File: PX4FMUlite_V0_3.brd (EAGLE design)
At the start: 48.6 x 34.9 mm, 143 parts, among them J2 DF13-4P-1.25V, J201 DF13C-6P-1.25V, J202 DF13C-6P-1.25V, J203 DF13C-6P-1.25V, J3 DF13C-4P-1.25V, J302 DF13C-4P-1.25V, J401 DF13C-4P-1.25V, J403 DF13C-7P-1.25V, J405 DF13C-4P-1.25V, J802 DF13C-3P-1.25V, M3_MOUNT1101 MOUNT-HOLE3.1MM, M3_MOUNT1102 MOUNT-HOLE3.1MM, M3_MOUNT1103 MOUNT-HOLE3.1MM, M3_MOUNT1104 MOUNT-HOLE3.1MM, U101 STM32F4X7VX, U2 MAX3051, U401 MAX3051, X101 3.2x2.5 mm / 24 MHz / 15 ppm

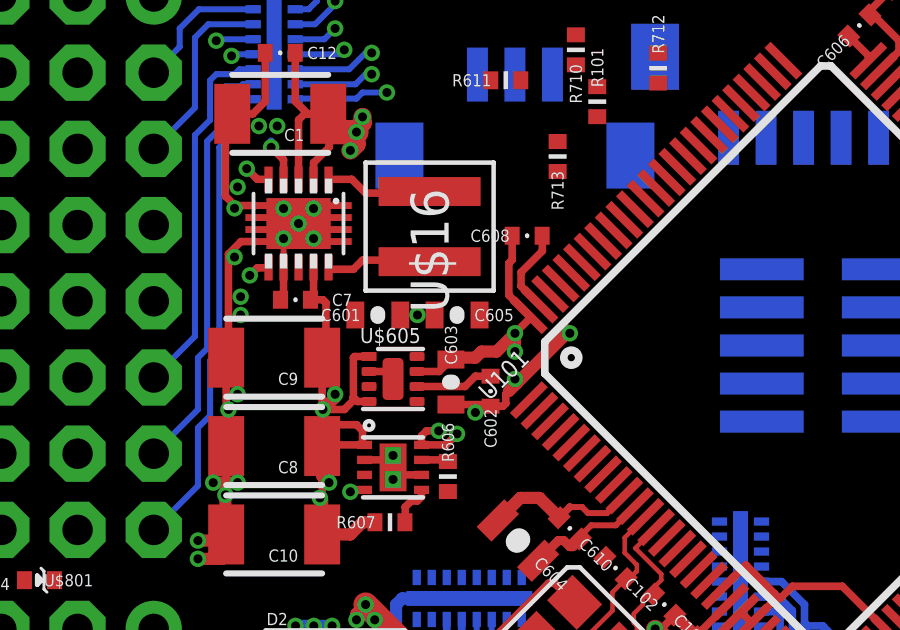
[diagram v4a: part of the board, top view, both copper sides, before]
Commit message: Spektrum 3V3 power routing half done
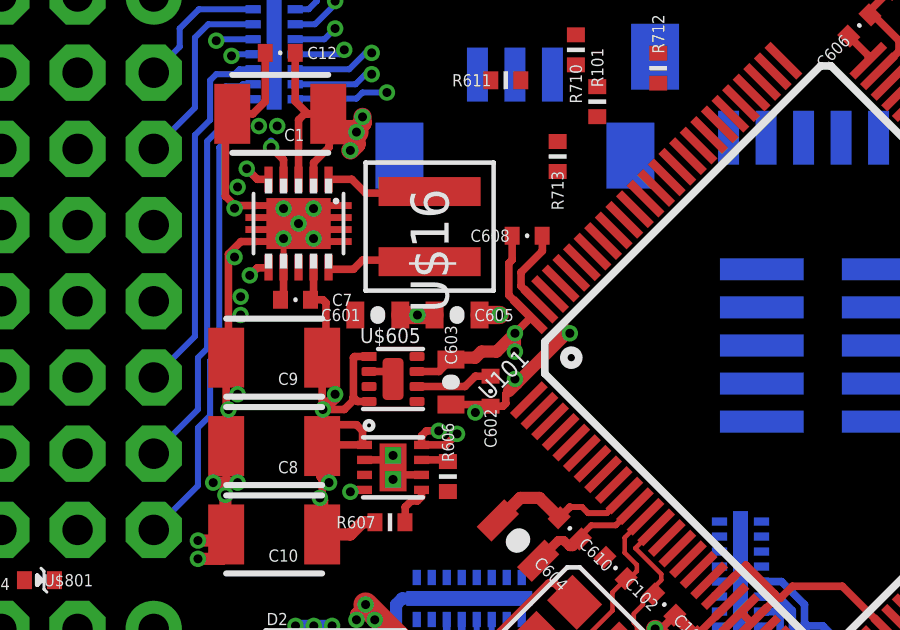
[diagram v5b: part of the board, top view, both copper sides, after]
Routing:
- net GND: track 122.7 -> 123.8 mm
- net VDD_3V3_SPEKTRUM: track 0.00 -> 0.67 mm, vias 0 -> 1
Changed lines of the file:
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@@
 <contactref element="U$801" pad="C"/>
 <contactref element="U$14" pad="2"/>
+<via x="27.5336" y="20.32" extent="1-16" drill="0.3"/>
+<wire x1="26.8612" y1="20.32" x2="27.5336" y2="20.32" width="0.6096" layer="1"/>
 <wire x1="24.7776" y1="18.9364" x2="26.8612" y2="20.32" width="0" layer="19" extent="1-1"/>
 <wire x1="12.692" y1="11.4808" x2="24.7776" y2="18.9364" width="0" layer="19" extent="1-1"/>
@@
 <wire x1="28.0416" y1="18.0848" x2="28.0924" y2="18.034" width="0.4064" layer="1"/>
 <wire x1="29.7688" y1="19.7104" x2="29.8704" y2="19.7104" width="0.4064" layer="1"/>
+<wire x1="19.9136" y1="8.4248" x2="19.0928" y2="8.4248" width="0.4064" layer="16"/>
+<wire x1="19.0928" y1="8.4248" x2="18.8976" y2="8.2296" width="0.4064" layer="16"/>
+<wire x1="18.8976" y1="8.2296" x2="18.8976" y2="7.4168" width="0.4064" layer="16"/>
+<wire x1="18.8976" y1="7.4168" x2="18.1864" y2="6.7056" width="0.4064" layer="16"/>
+<wire x1="18.1864" y1="6.7056" x2="17.0688" y2="6.7056" width="0.4064" layer="16"/>
+<wire x1="20.936" y1="8.128" x2="20.6248" y2="8.128" width="0.3048" layer="16"/>
+<wire x1="20.6248" y1="8.128" x2="20.328" y2="8.4248" width="0.3048" layer="16"/>
+<wire x1="20.328" y1="8.4248" x2="19.9136" y2="8.4248" width="0.3048" layer="16"/>
+<wire x1="24.2196" y1="20.32" x2="25.3612" y2="20.32" width="0.6096" layer="1"/>
 <wire x1="101.4292" y1="51.6128" x2="99.1696" y2="57.3024" width="0" layer="19" extent="1-1"/>
 <wire x1="88.134" y1="27.1144" x2="101.4292" y2="51.6128" width="0" layer="19" extent="1-1"/>
@@
 <wire x1="24.2196" y1="20.32" x2="23.9776" y2="18.4364" width="0" layer="19" extent="1-1"/>
 <wire x1="24.7904" y1="20.32" x2="24.2196" y2="20.32" width="0" layer="19" extent="1-1"/>
-<wire x1="25.3612" y1="20.32" x2="24.7904" y2="20.32" width="0" layer="19" extent="1-1"/>
 <wire x1="22.253" y1="22.768" x2="24.2196" y2="20.32" width="0" layer="19" extent="1-1"/>
 <wire x1="22.253" y1="23.168" x2="22.253" y2="22.768" width="0" layer="19" extent="1-1"/>
@@
 <wire x1="31.0896" y1="60.3504" x2="31.0896" y2="58.428" width="0" layer="19" extent="1-16"/>
 <wire x1="16.3656" y1="66.6496" x2="31.0896" y2="60.3504" width="0" layer="19" extent="1-16"/>
-<wire x1="19.9136" y1="8.4248" x2="19.0928" y2="8.4248" width="0.4064" layer="16"/>
-<wire x1="19.0928" y1="8.4248" x2="18.8976" y2="8.2296" width="0.4064" layer="16"/>
-<wire x1="18.8976" y1="8.2296" x2="18.8976" y2="7.4168" width="0.4064" layer="16"/>
-<wire x1="18.8976" y1="7.4168" x2="18.1864" y2="6.7056" width="0.4064" layer="16"/>
-<wire x1="18.1864" y1="6.7056" x2="17.0688" y2="6.7056" width="0.4064" layer="16"/>
-<wire x1="20.936" y1="8.128" x2="20.6248" y2="8.128" width="0.3048" layer="16"/>
-<wire x1="20.6248" y1="8.128" x2="20.328" y2="8.4248" width="0.3048" layer="16"/>
-<wire x1="20.328" y1="8.4248" x2="19.9136" y2="8.4248" width="0.3048" layer="16"/>
 </signal>
 <signal name="N$4">

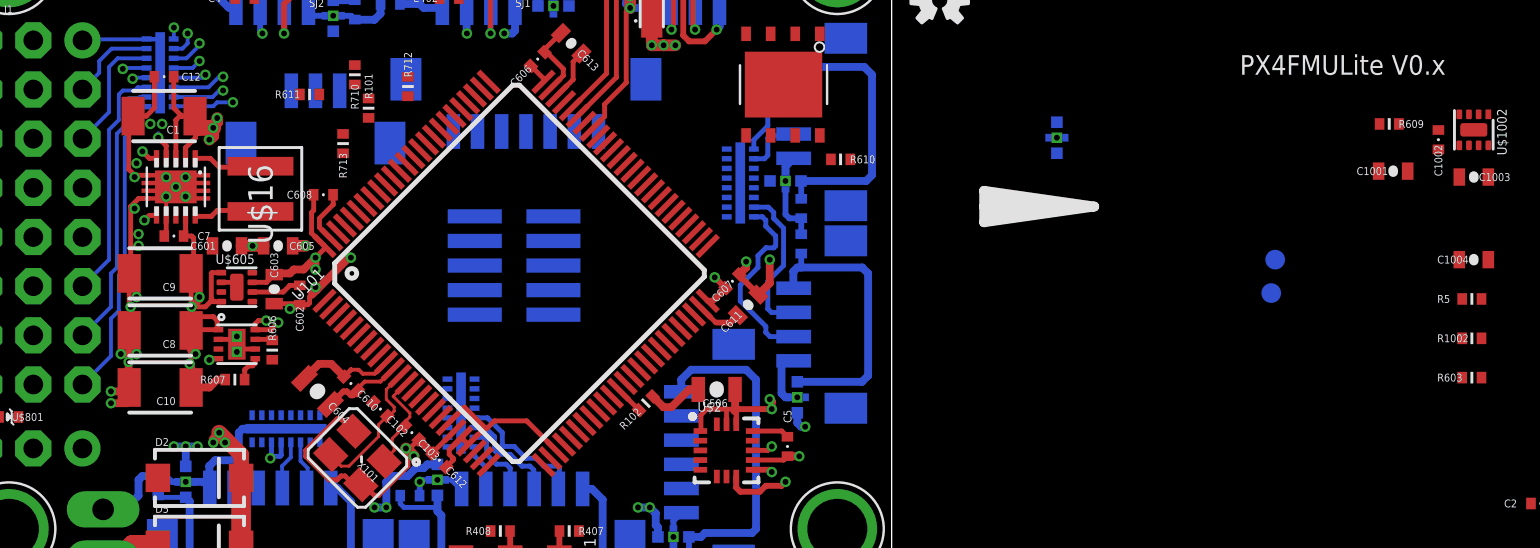
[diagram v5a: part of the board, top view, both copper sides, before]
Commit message: Tweaks to FMU 5V LDO layout
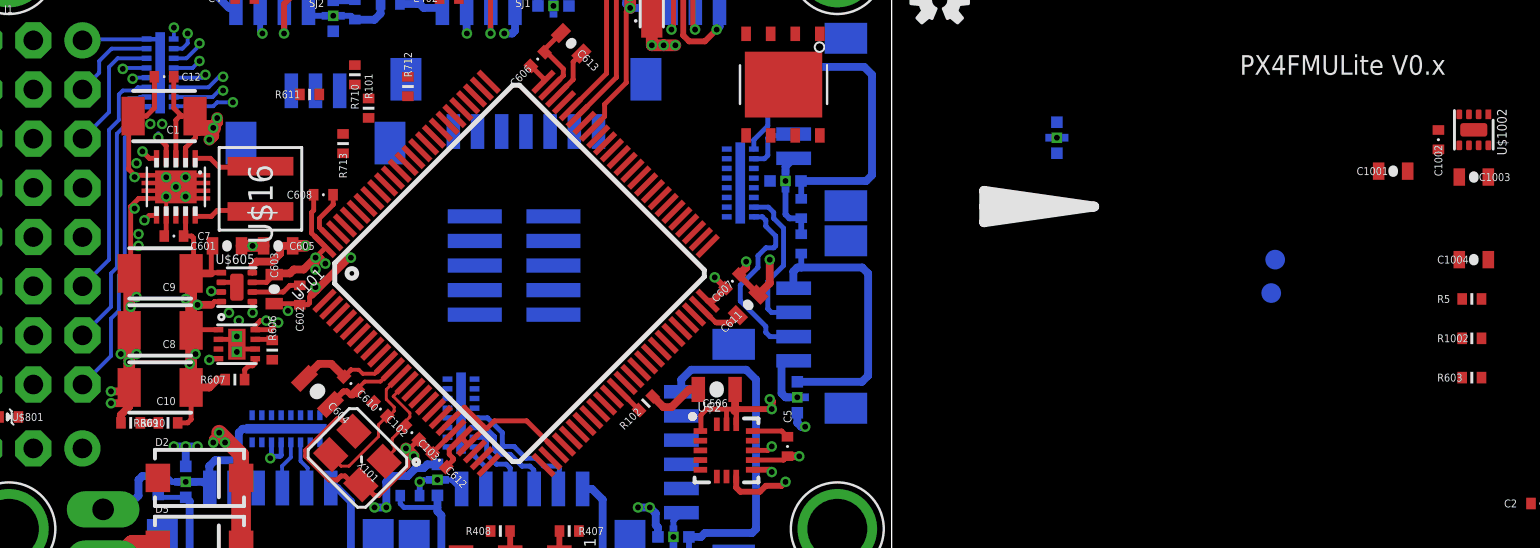
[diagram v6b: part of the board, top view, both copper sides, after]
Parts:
- moved R609 65.0 mm to (20.4, 11.2), turned to 0 degrees
- moved R610 39.1 mm to (18.5, 11.2)
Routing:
- net VDD_5V: track 19.7 -> 23.4 mm
- net VDD_3V3_SPEKTRUM: track 0.67 -> 3.72 mm
- net N$5: track 1.30 -> 0.00 mm
- net VDD_5V_SENS: track 0.00 -> 0.93 mm
- net FMU-VDD_3V3: track 32.9 -> 33.5 mm, vias 3 -> 4
- net VDD_3V3_SPEKTRUM_EN: track 0.00 -> 0.58 mm, vias 0 -> 1
- net FMU-!RESET: track 0.00 -> 0.54 mm, vias 0 -> 1
- net GND: track 123.8 -> 124.4 mm, vias 27 -> 29

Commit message: More power routing
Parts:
- removed R101: 470R, pixhawk2:0402-RES
- moved L402 20.2 mm to (46.2, 27.1), turned to 0 degrees
- moved R713 3.74 mm to (26.8, 28.2), turned to 270 degrees
- moved R611 3.53 mm to (28.4, 24.7)
- moved R710 0.72 mm to (30.8, 29.1)
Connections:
- removed net IO-USART1_RX: L3.P$4
- removed net IO-USART1_TX: R101.P$2
- removed net N$23: R101.P$1, U101.69
- new net SPEKTRUM_RX: L3.P$4, U101.69
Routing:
- net N$41: track 0.00 -> 17.9 mm
- net GND: track 124.4 -> 130.6 mm, vias 29 -> 30
- net VDD_5V_PERIPH: track 64.8 -> 67.4 mm, vias 10 -> 13
- net VDD_IN: track 67.0 -> 66.1 mm

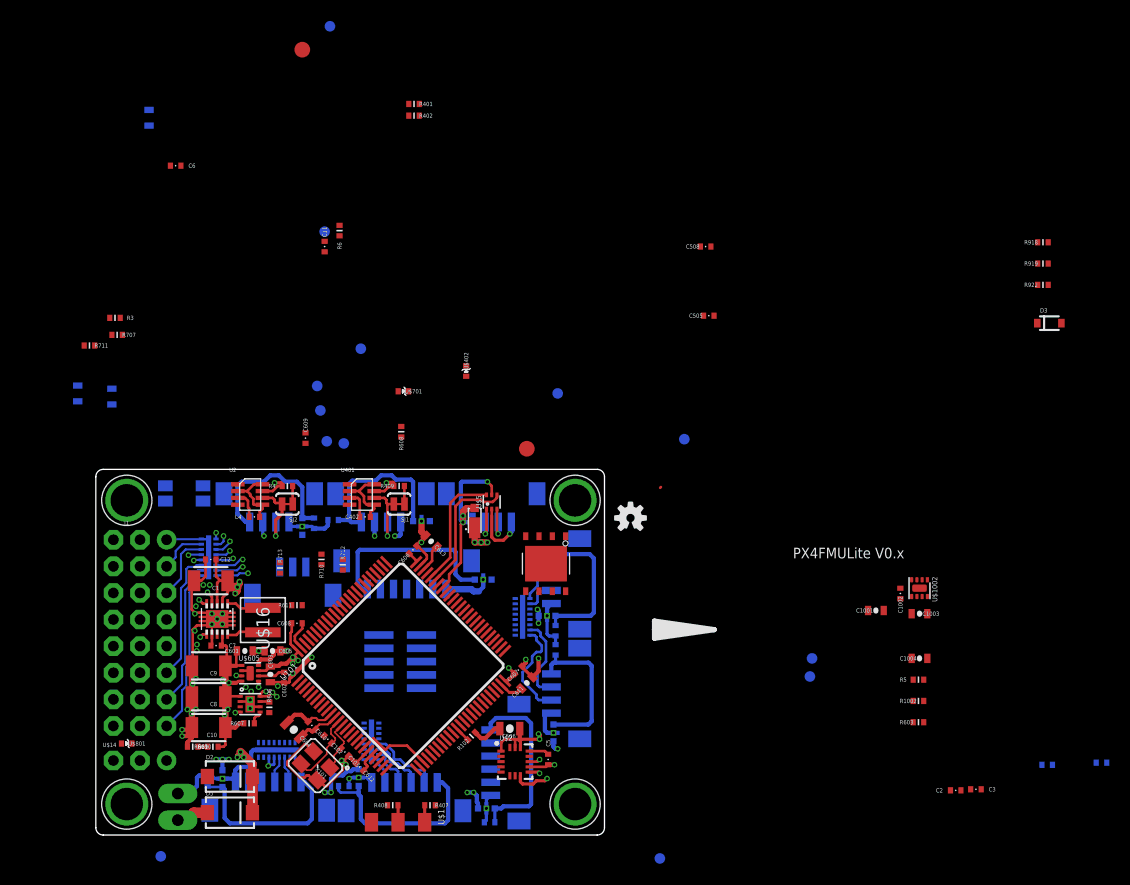
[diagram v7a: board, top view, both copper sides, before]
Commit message: More power routing.  flash placed and part routed
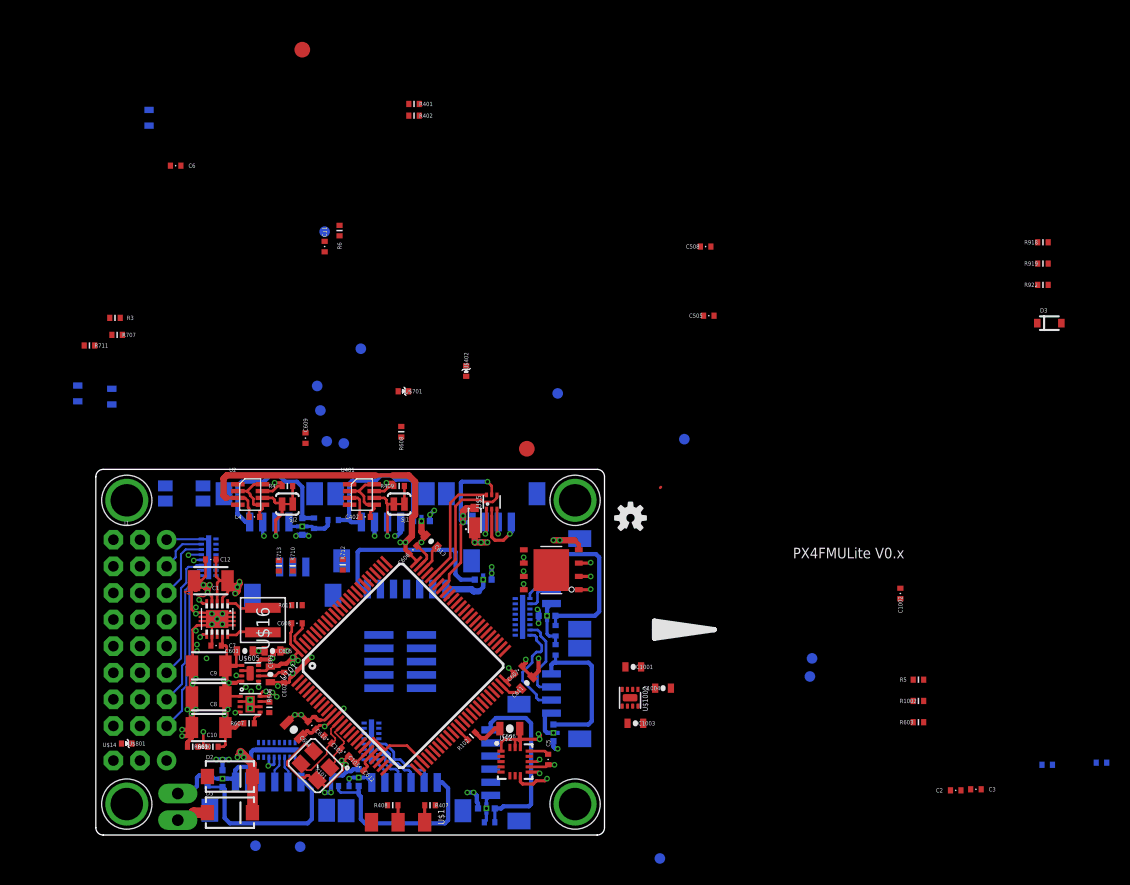
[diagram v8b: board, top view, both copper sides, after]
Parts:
- moved S3RX 78.6 mm to (24.5, 1.73), turned to 0 degrees
- moved U$1002 29.6 mm to (60.2, 15.8)
- moved C1003 29.1 mm to (60.8, 13.4)
- moved C1004 24.7 mm to (63.4, 16.8)
- moved C1001 23.8 mm to (60.6, 18.8), turned to 180 degrees
- moved S3TX 13.3 mm to (28.8, 1.63)
- moved R710 2.81 mm to (28.0, 28.4), turned to 270 degrees
- moved U$3 0.79 mm to (52.7, 28.0), turned to 90 degrees
- moved R713 0.23 mm to (26.7, 28.4)
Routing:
- net FMU-VDD_3V3: track 33.5 -> 64.9 mm, vias 4 -> 9
- net VDD_3V3_SPEKTRUM: track 3.72 -> 28.9 mm, vias 1 -> 3
- net VDD_5V_PERIPH: track 67.4 -> 89.0 mm, vias 13 -> 19
- net GND: track 130.6 -> 136.3 mm, vias 30 -> 34
- net FMU-CH8: track 3.97 -> 0.00 mm, vias 1 -> 0
- net VDD_IN: track 66.1 -> 69.9 mm
- net FMU-CH7: track 3.81 -> 0.00 mm, vias 1 -> 0
- net FMU-CH5: track 3.33 -> 0.00 mm, vias 1 -> 0
- net FMU-CH6: track 3.10 -> 0.00 mm, vias 1 -> 0
- net FMU-CH4: track 2.56 -> 0.00 mm, vias 1 -> 0
- net FMU-CH3: track 1.86 -> 0.00 mm, vias 1 -> 0
- net VDD_5V_SENS: track 0.93 -> 2.77 mm, vias 0 -> 1
- net FMU-CH2: track 1.75 -> 0.00 mm, vias 1 -> 0
- net SDIO_CMD: track 0.00 -> 1.15 mm, vias 0 -> 1
- net SDIO_D2: track 0.00 -> 1.15 mm, vias 0 -> 1
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- added copper zone on layer 15, net FMU-VDD_3V3
- added copper zone on layer 1, net GND
